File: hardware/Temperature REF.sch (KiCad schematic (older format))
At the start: 15 parts

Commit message: Assigning footprints
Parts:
- C51, C52, C53, C54, C55, C56, C57, C58, C59: renamed from C?; footprint (none) -> Capacitor_SMD:C_0603_1608Metric
- R10, R11, R12, R13: renamed from R?; footprint (none) -> Resistor_SMD:R_0805_2012Metric
- gave numbers to parts that had none: 2
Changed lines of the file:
@@
 P 5700 1750
 AR Path="/5E22D897/5E7732A9" Ref="U?"  Part="1"
-AR Path="/5E22D897/5E7660D0/5E7732A9" Ref="U?"  Part="1"
-F 0 "U?" H 5700 2420 50  0000 C CNN
+AR Path="/5E22D897/5E7660D0/5E7732A9" Ref="U5"  Part="1"
+F 0 "U5" H 5700 2420 50  0000 C CNN
 F 1 "OPA2211AIDDA" H 5700 2329 50  0000 C CNN
 F 2 "OPA2211:SOIC127P600X170-9N" H 5700 1750 50  0001 L BNN
@@
 P 2150 1750
 AR Path="/5E22D897/5E7732B0" Ref="U?"  Part="1"
-AR Path="/5E22D897/5E7660D0/5E7732B0" Ref="U?"  Part="1"
-F 0 "U?" H 2150 2228 50  0000 C CNN
+AR Path="/5E22D897/5E7660D0/5E7732B0" Ref="U2"  Part="1"
+F 0 "U2" H 2150 2228 50  0000 C CNN
 F 1 "REF5025AD" H 2150 2137 50  0000 C CNN
 F 2 "Package_SO:SOIC-8_3.9x4.9mm_P1.27mm" H 2075 1500 50  0001 L CIN
@@
 P 900 1800
 AR Path="/5E22D897/5E7732B7" Ref="C?"  Part="1"
-AR Path="/5E22D897/5E7660D0/5E7732B7" Ref="C?"  Part="1"
-F 0 "C?" H 1015 1846 50  0000 L CNN
+AR Path="/5E22D897/5E7660D0/5E7732B7" Ref="C51"  Part="1"
+F 0 "C51" H 1015 1846 50  0000 L CNN
 F 1 "10uF" H 1015 1755 50  0000 L CNN
-F 2 "" H 938 1650 50  0001 C CNN
+F 2 "Capacitor_SMD:C_0603_1608Metric" H 938 1650 50  0001 C CNN
 F 3 "~" H 900 1800 50  0001 C CNN
 	1    900  1800
@@
 P 1300 1800
 AR Path="/5E22D897/5E7732BE" Ref="C?"  Part="1"
-AR Path="/5E22D897/5E7660D0/5E7732BE" Ref="C?"  Part="1"
-F 0 "C?" H 1415 1846 50  0000 L CNN
+AR Path="/5E22D897/5E7660D0/5E7732BE" Ref="C52"  Part="1"
+F 0 "C52" H 1415 1846 50  0000 L CNN
 F 1 "100n" H 1415 1755 50  0000 L CNN
-F 2 "" H 1338 1650 50  0001 C CNN
+F 2 "Capacitor_SMD:C_0603_1608Metric" H 1338 1650 50  0001 C CNN
 F 3 "~" H 1300 1800 50  0001 C CNN
 	1    1300 1800
@@
 P 2700 2100
 AR Path="/5E22D897/5E7732DB" Ref="C?"  Part="1"
-AR Path="/5E22D897/5E7660D0/5E7732DB" Ref="C?"  Part="1"
-F 0 "C?" H 2815 2146 50  0000 L CNN
+AR Path="/5E22D897/5E7660D0/5E7732DB" Ref="C53"  Part="1"
+F 0 "C53" H 2815 2146 50  0000 L CNN
 F 1 "1u" H 2815 2055 50  0000 L CNN
-F 2 "" H 2738 1950 50  0001 C CNN
+F 2 "Capacitor_SMD:C_0603_1608Metric" H 2738 1950 50  0001 C CNN
 F 3 "~" H 2700 2100 50  0001 C CNN
 	1    2700 2100
@@
 P 3050 1850
 AR Path="/5E22D897/5E7732E6" Ref="R?"  Part="1"
-AR Path="/5E22D897/5E7660D0/5E7732E6" Ref="R?"  Part="1"
-F 0 "R?" H 3120 1896 50  0000 L CNN
+AR Path="/5E22D897/5E7660D0/5E7732E6" Ref="R10"  Part="1"
+F 0 "R10" H 3120 1896 50  0000 L CNN
 F 1 "1R" H 3120 1805 50  0000 L CNN
-F 2 "" V 2980 1850 50  0001 C CNN
+F 2 "Resistor_SMD:R_0805_2012Metric" V 2980 1850 50  0001 C CNN
 F 3 "~" H 3050 1850 50  0001 C CNN
 	1    3050 1850
@@
 P 3050 2200
 AR Path="/5E22D897/5E7732ED" Ref="C?"  Part="1"
-AR Path="/5E22D897/5E7660D0/5E7732ED" Ref="C?"  Part="1"
-F 0 "C?" H 3165 2246 50  0000 L CNN
+AR Path="/5E22D897/5E7660D0/5E7732ED" Ref="C54"  Part="1"
+F 0 "C54" H 3165 2246 50  0000 L CNN
 F 1 "22u" H 3165 2155 50  0000 L CNN
-F 2 "" H 3088 2050 50  0001 C CNN
+F 2 "Capacitor_SMD:C_0603_1608Metric" H 3088 2050 50  0001 C CNN
 F 3 "~" H 3050 2200 50  0001 C CNN
 	1    3050 2200
@@
 P 3450 1650
 AR Path="/5E22D897/5E7732F9" Ref="R?"  Part="1"
-AR Path="/5E22D897/5E7660D0/5E7732F9" Ref="R?"  Part="1"
-F 0 "R?" V 3243 1650 50  0000 C CNN
+AR Path="/5E22D897/5E7660D0/5E7732F9" Ref="R11"  Part="1"
+F 0 "R11" V 3243 1650 50  0000 C CNN
 F 1 "10R" V 3334 1650 50  0000 C CNN
-F 2 "" V 3380 1650 50  0001 C CNN
+F 2 "Resistor_SMD:R_0805_2012Metric" V 3380 1650 50  0001 C CNN
 F 3 "~" H 3450 1650 50  0001 C CNN
 	1    3450 1650
@@
 P 3700 2000
 AR Path="/5E22D897/5E773302" Ref="C?"  Part="1"
-AR Path="/5E22D897/5E7660D0/5E773302" Ref="C?"  Part="1"
-F 0 "C?" H 3815 2046 50  0000 L CNN
+AR Path="/5E22D897/5E7660D0/5E773302" Ref="C55"  Part="1"
+F 0 "C55" H 3815 2046 50  0000 L CNN
 F 1 "47u" H 3815 1955 50  0000 L CNN
-F 2 "" H 3738 1850 50  0001 C CNN
+F 2 "Capacitor_SMD:C_0603_1608Metric" H 3738 1850 50  0001 C CNN
 F 3 "~" H 3700 2000 50  0001 C CNN
 	1    3700 2000
@@
 P 4000 2000
 AR Path="/5E22D897/5E773309" Ref="C?"  Part="1"
-AR Path="/5E22D897/5E7660D0/5E773309" Ref="C?"  Part="1"
-F 0 "C?" H 4115 2046 50  0000 L CNN
+AR Path="/5E22D897/5E7660D0/5E773309" Ref="C56"  Part="1"
+F 0 "C56" H 4115 2046 50  0000 L CNN
 F 1 "47u" H 4115 1955 50  0000 L CNN
-F 2 "" H 4038 1850 50  0001 C CNN
+F 2 "Capacitor_SMD:C_0603_1608Metric" H 4038 1850 50  0001 C CNN
 F 3 "~" H 4000 2000 50  0001 C CNN
 	1    4000 2000
@@
 P 4300 2000
 AR Path="/5E22D897/5E773310" Ref="C?"  Part="1"
-AR Path="/5E22D897/5E7660D0/5E773310" Ref="C?"  Part="1"
-F 0 "C?" H 4415 2046 50  0000 L CNN
+AR Path="/5E22D897/5E7660D0/5E773310" Ref="C57"  Part="1"
+F 0 "C57" H 4415 2046 50  0000 L CNN
 F 1 "10n" H 4415 1955 50  0000 L CNN
-F 2 "" H 4338 1850 50  0001 C CNN
+F 2 "Capacitor_SMD:C_0603_1608Metric" H 4338 1850 50  0001 C CNN
 F 3 "~" H 4300 2000 50  0001 C CNN
 	1    4300 2000
@@
 P 6600 1750
 AR Path="/5E22D897/5E77332E" Ref="C?"  Part="1"
-AR Path="/5E22D897/5E7660D0/5E77332E" Ref="C?"  Part="1"
-F 0 "C?" H 6715 1796 50  0000 L CNN
+AR Path="/5E22D897/5E7660D0/5E77332E" Ref="C58"  Part="1"
+F 0 "C58" H 6715 1796 50  0000 L CNN
 F 1 "10n" H 6715 1705 50  0000 L CNN
-F 2 "" H 6638 1600 50  0001 C CNN
+F 2 "Capacitor_SMD:C_0603_1608Metric" H 6638 1600 50  0001 C CNN
 F 3 "~" H 6600 1750 50  0001 C CNN
 	1    6600 1750
@@
 P 6850 2600
 AR Path="/5E22D897/5E773339" Ref="R?"  Part="1"
-AR Path="/5E22D897/5E7660D0/5E773339" Ref="R?"  Part="1"
-F 0 "R?" V 6643 2600 50  0000 C CNN
+AR Path="/5E22D897/5E7660D0/5E773339" Ref="R13"  Part="1"
+F 0 "R13" V 6643 2600 50  0000 C CNN
 F 1 "49R9" V 6734 2600 50  0000 C CNN
-F 2 "" V 6780 2600 50  0001 C CNN
+F 2 "Resistor_SMD:R_0805_2012Metric" V 6780 2600 50  0001 C CNN
 F 3 "~" H 6850 2600 50  0001 C CNN
 	1    6850 2600
@@
 P 6800 1450
 AR Path="/5E22D897/5E773344" Ref="R?"  Part="1"
-AR Path="/5E22D897/5E7660D0/5E773344" Ref="R?"  Part="1"
-F 0 "R?" V 6593 1450 50  0000 C CNN
+AR Path="/5E22D897/5E7660D0/5E773344" Ref="R12"  Part="1"
+F 0 "R12" V 6593 1450 50  0000 C CNN
 F 1 "100R" V 6684 1450 50  0000 C CNN
-F 2 "" V 6730 1450 50  0001 C CNN
+F 2 "Resistor_SMD:R_0805_2012Metric" V 6730 1450 50  0001 C CNN
 F 3 "~" H 6800 1450 50  0001 C CNN
 	1    6800 1450
@@
 P 7250 2000
 AR Path="/5E22D897/5E77334E" Ref="C?"  Part="1"
-AR Path="/5E22D897/5E7660D0/5E77334E" Ref="C?"  Part="1"
-F 0 "C?" H 7365 2046 50  0000 L CNN
+AR Path="/5E22D897/5E7660D0/5E77334E" Ref="C59"  Part="1"
+F 0 "C59" H 7365 2046 50  0000 L CNN
 F 1 "47u" H 7365 1955 50  0000 L CNN
-F 2 "" H 7288 1850 50  0001 C CNN
+F 2 "Capacitor_SMD:C_0603_1608Metric" H 7288 1850 50  0001 C CNN
 F 3 "~" H 7250 2000 50  0001 C CNN
 	1    7250 2000

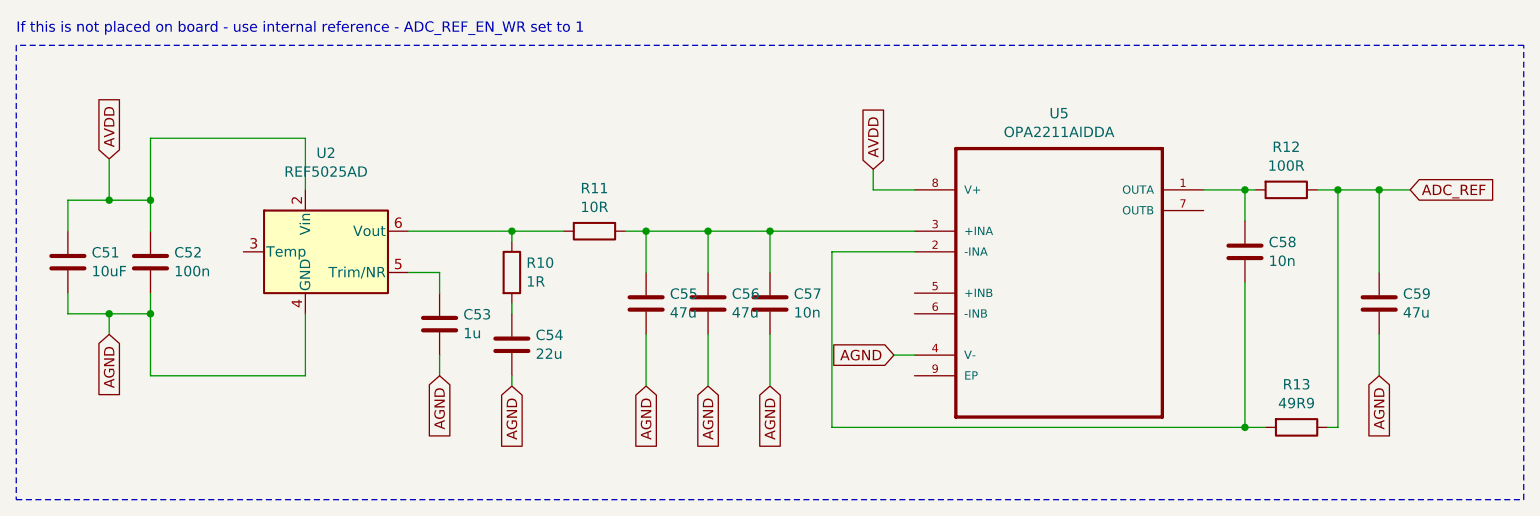
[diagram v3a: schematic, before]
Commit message: Renaming wires
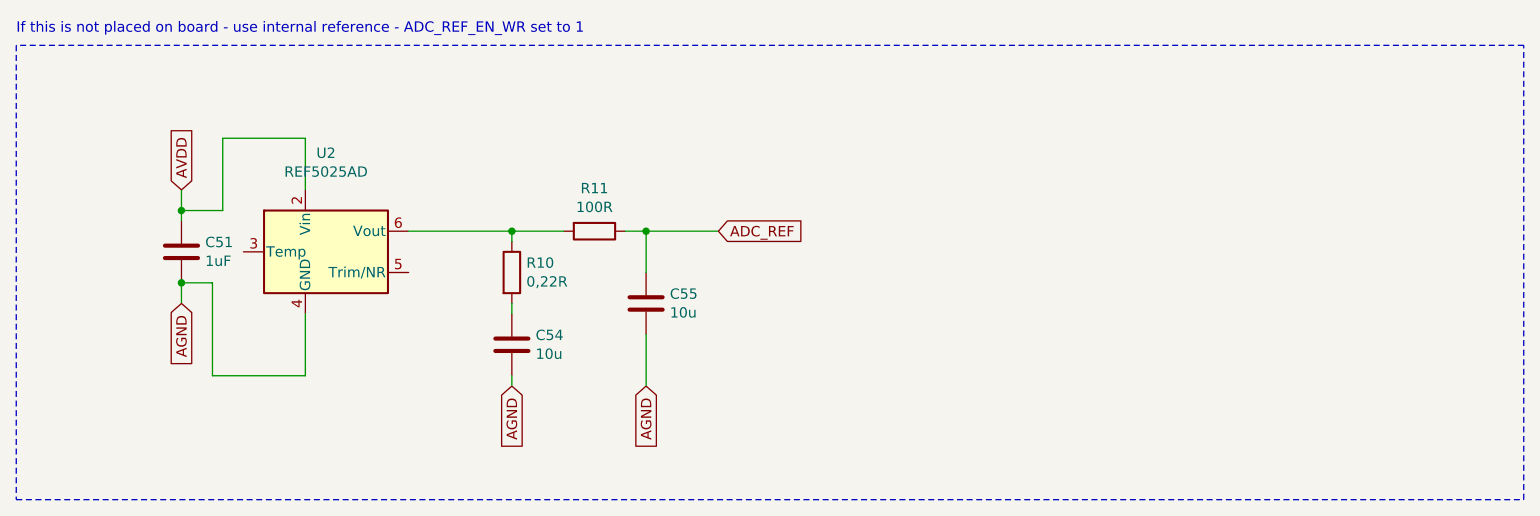
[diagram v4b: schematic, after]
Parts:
- removed C52: 100n, Capacitor_SMD:C_0603_1608Metric, symbol antena:C
- removed C53: 1u, Capacitor_SMD:C_0603_1608Metric, symbol antena:C
- removed C56, C59: 47u, Capacitor_SMD:C_0603_1608Metric, symbol antena:C
- removed C57, C58: 10n, Capacitor_SMD:C_0603_1608Metric, symbol antena:C
- removed R12: 100R, Resistor_SMD:R_0805_2012Metric, symbol antena:R
- removed R13: 49R9, Resistor_SMD:R_0805_2012Metric, symbol antena:R
- removed U5: OPA2211AIDDA, OPA2211:SOIC127P600X170-9N, symbol OPA2211AIDDA:OPA2211AIDDA
- C51: value 10uF -> 1uF
- C54: value 22u -> 10u
- C55: value 47u -> 10u
- R10: value 1R -> 0,22R
- R11: value 10R -> 100R
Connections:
- net ADC_REF: now also C55.1, R11.1
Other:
- moved on the sheet: C51

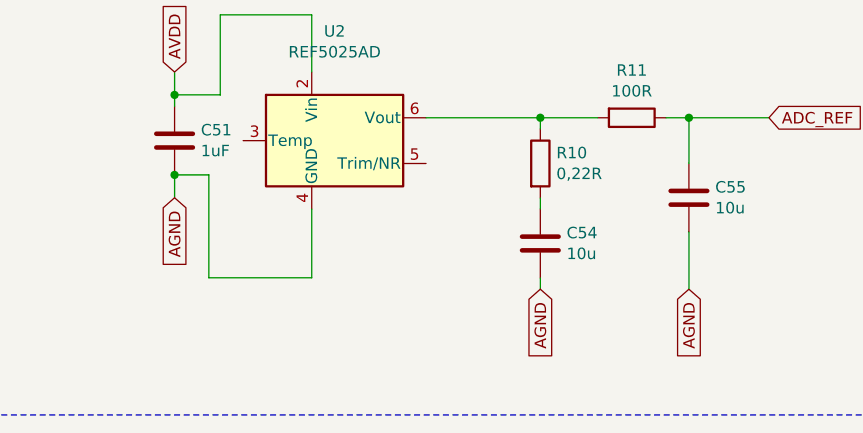
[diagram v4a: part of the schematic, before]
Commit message: Finishing routing
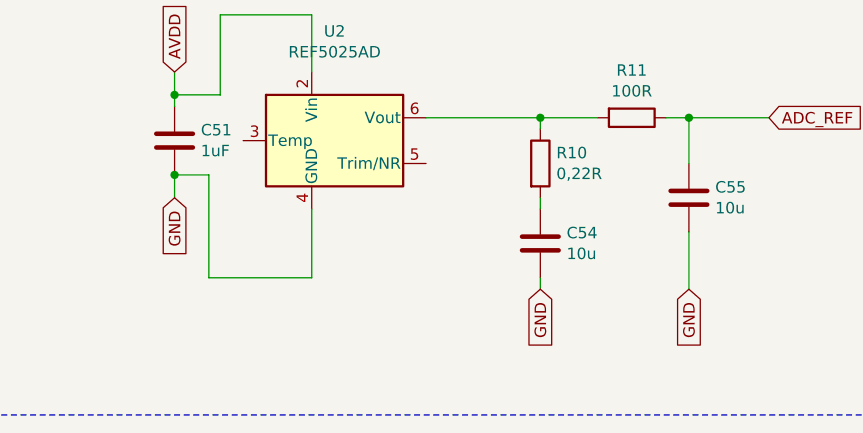
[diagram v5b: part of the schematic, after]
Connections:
- net AGND renamed GND
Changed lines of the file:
@@
 	1450 1900 1450 2000
 Text GLabel 1450 2000 3    50   Input ~ 0
-AGND
+GND
 Text GLabel 1450 1450 1    50   Input ~ 0
 AVDD
@@
 	3050 2000 3050 2050
 Text GLabel 3050 2400 3    50   Input ~ 0
-AGND
+GND
 Wire Wire Line
 	3050 2350 3050 2400
@@
 	3700 1650 3700 1850
 Text GLabel 3700 2400 3    50   Input ~ 0
-AGND
+GND
 Wire Wire Line
 	3700 2150 3700 2400

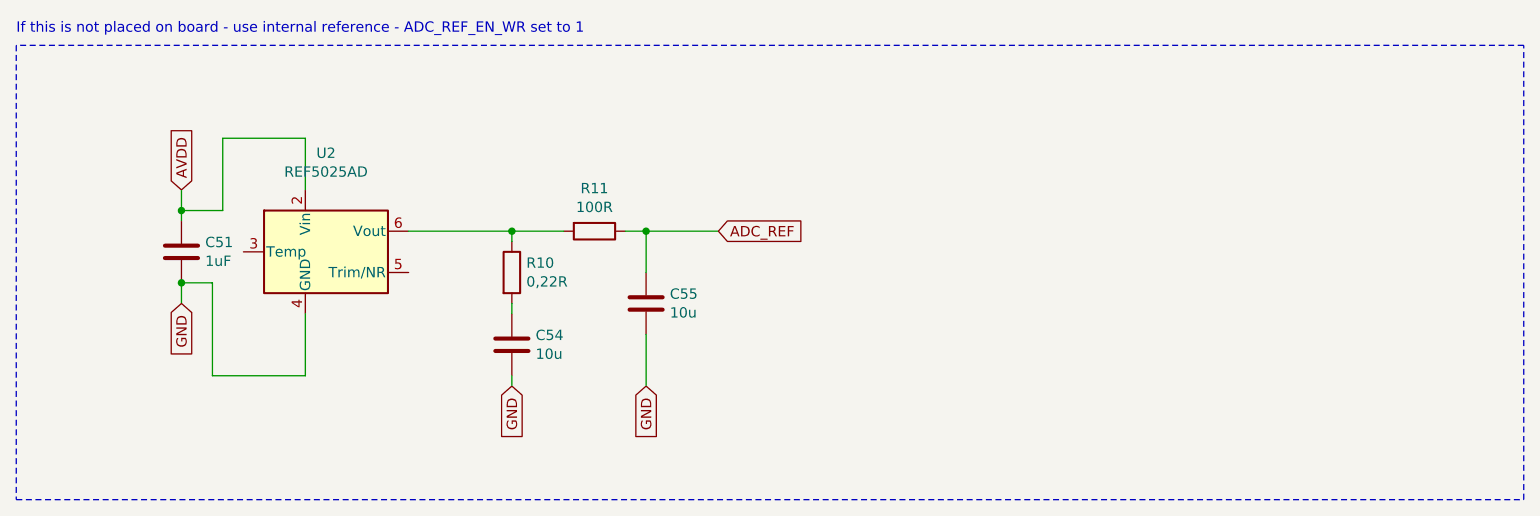
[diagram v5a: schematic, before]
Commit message: Adding pcb changes to PBC
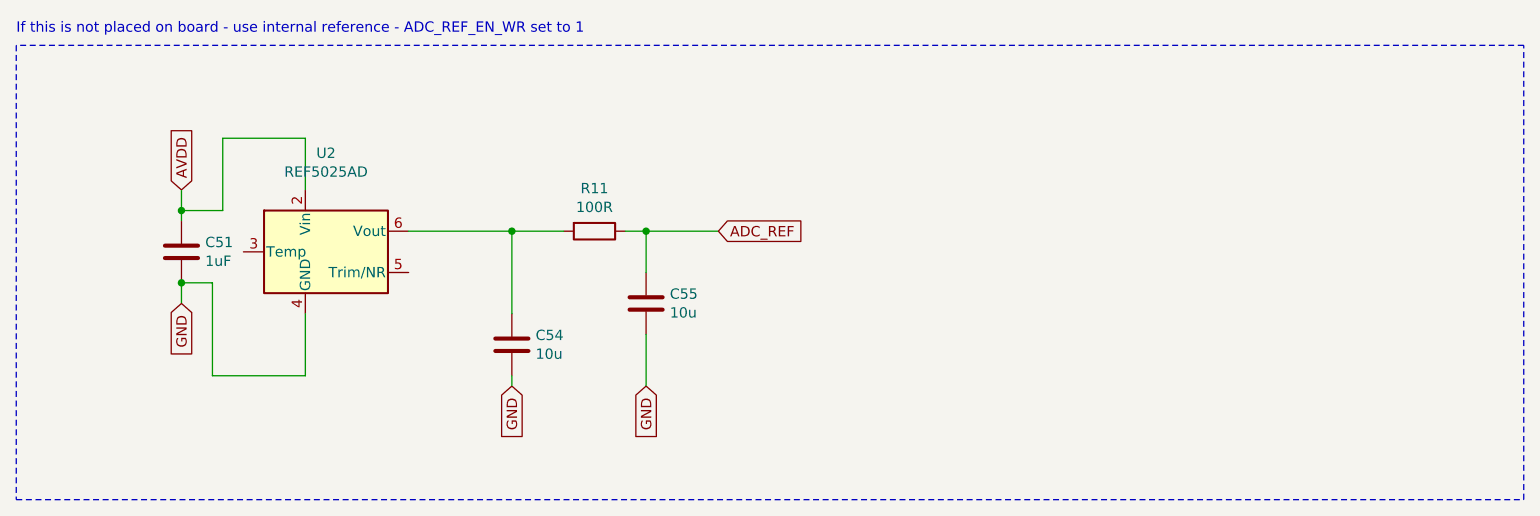
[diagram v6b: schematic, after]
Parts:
- removed R10: 0,22R, Resistor_SMD:R_0805_2012Metric, symbol antena:R
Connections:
- net at R11.2, U2.6 (Vout): now also C54.1
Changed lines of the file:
@@
 	2050 2350 2050 2050
-$Comp
-L antena:R R?
-U 1 1 5E7732E6
-P 3050 1850
-AR Path="/5E22D897/5E7732E6" Ref="R?"  Part="1"
-AR Path="/5E22D897/5E7660D0/5E7732E6" Ref="R10"  Part="1"
-F 0 "R10" H 3120 1896 50  0000 L CNN
-F 1 "0,22R" H 3120 1805 50  0000 L CNN
-F 2 "Resistor_SMD:R_0805_2012Metric" V 2980 1850 50  0001 C CNN
-F 3 "~" H 3050 1850 50  0001 C CNN
-	1    3050 1850
-	1    0    0    -1
-$EndComp
 $Comp
 L antena:C C?
@@
 $EndComp
 Wire Wire Line
-	3050 1650 3050 1700
-Wire Wire Line
 	2550 1650 3050 1650
-Wire Wire Line
-	3050 2000 3050 2050
 Text GLabel 3050 2400 3    50   Input ~ 0
 GND
@@
 	1600 2350 2050 2350
 Connection ~ 1450 1900
+Wire Wire Line
+	3050 1650 3050 2050
 $EndSCHEMATC

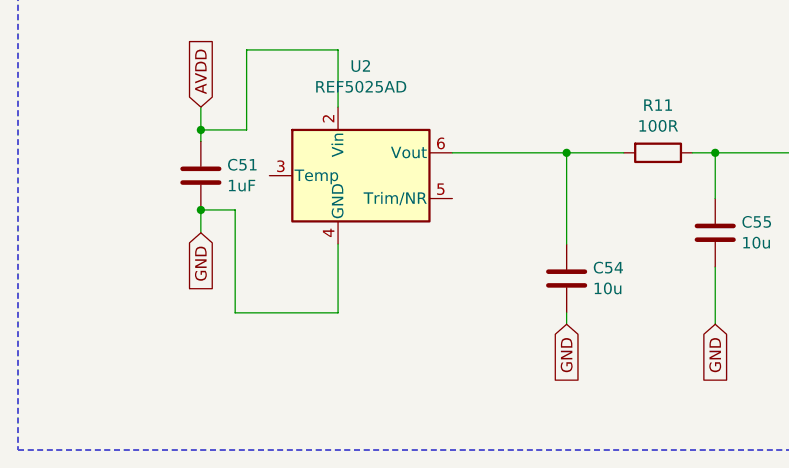
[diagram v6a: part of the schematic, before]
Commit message: Rerouting
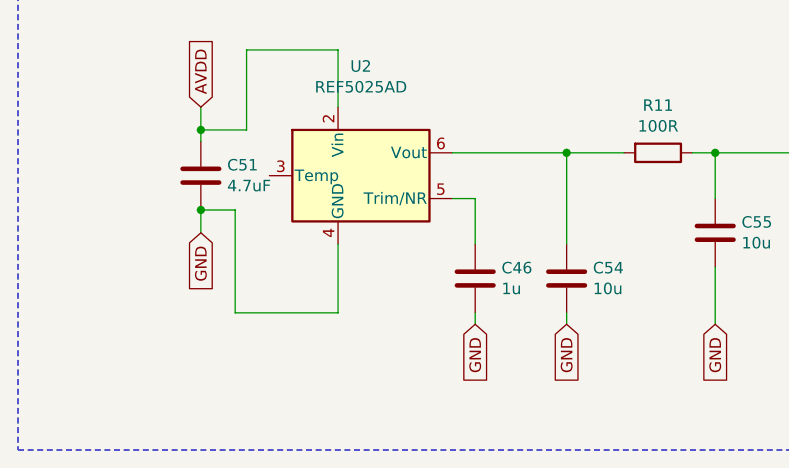
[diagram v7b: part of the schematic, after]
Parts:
- added C46: 1u, Capacitor_SMD:C_0603_1608Metric, symbol antena:C
- C51: value 1uF -> 4.7uF
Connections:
- net GND: now also C46.2
- net at U2.5 (Trim/NR): now also C46.1
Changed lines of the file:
@@
 AR Path="/5E22D897/5E7660D0/5E7732B7" Ref="C51"  Part="1"
 F 0 "C51" H 1565 1796 50  0000 L CNN
-F 1 "1uF" H 1565 1705 50  0000 L CNN
+F 1 "4.7uF" H 1565 1705 50  0000 L CNN
 F 2 "Capacitor_SMD:C_0603_1608Metric" H 1488 1600 50  0001 C CNN
 F 3 "~" H 1450 1750 50  0001 C CNN
@@
 Wire Wire Line
 	3050 1650 3050 2050
+$Comp
+L antena:C C?
+U 1 1 5E45474B
+P 2650 2200
+AR Path="/5E22D897/5E45474B" Ref="C?"  Part="1"
+AR Path="/5E22D897/5E7660D0/5E45474B" Ref="C46"  Part="1"
+F 0 "C46" H 2765 2246 50  0000 L CNN
+F 1 "1u" H 2765 2155 50  0000 L CNN
+F 2 "Capacitor_SMD:C_0603_1608Metric" H 2688 2050 50  0001 C CNN
+F 3 "~" H 2650 2200 50  0001 C CNN
+	1    2650 2200
+	1    0    0    -1
+$EndComp
+Wire Wire Line
+	2550 1850 2650 1850
+Wire Wire Line
+	2650 1850 2650 2050
+Text GLabel 2650 2400 3    50   Input ~ 0
+GND
+Wire Wire Line
+	2650 2400 2650 2350
 $EndSCHEMATC
